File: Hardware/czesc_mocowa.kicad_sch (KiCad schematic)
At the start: 20 parts, among them J1 Screw_Terminal_01x02, J2 Screw_Terminal_01x02, Q1 NMOS, Q2 NMOS, Q3 NMOS, Q4 NMOS, U1 IR2102, U2 IR2102

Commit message: Schemat-update
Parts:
- added C4: C_Polarized, symbol Device:C_Polarized
- added C5, C6: C, symbol Device:C
- added C7: 1nF, symbol Device:C
- added D3: C4D02120A, Package_TO_SOT_THT:TO-220-2_Vertical, symbol Diode:C4D02120A
- added Q5: BC547, Package_TO_SOT_THT:TO-92_Inline, symbol Transistor_BJT:BC547
- added R8: 330R, symbol Device:R
- added U3: LM780_TO220_MA BYC_3V_BO_POJDZIE_Z_DYMEM, Package_TO_SOT_THT:TO-220-3_Vertical, symbol Regulator_Linear:LM7805_TO220
- added U4: STM32L432KCUx, Package_DFN_QFN:QFN-32-1EP_5x5mm_P0.5mm_EP3.45x3.45mm, symbol MCU_ST_STM32L4:STM32L432KCUx
- added U5: ESP32-WROOM-32, RF_Module:ESP32-WROOM-32, symbol RF_Module:ESP32-WROOM-32
- renumbered J1 to WEJ_48V_DC, J2 to WYJSCIE
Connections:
- net GND: now also C3.2, C4.2, C5.2, C6.2, C7.1, Q5.3 (E), U3.2 (GND), U4.16 (VSS), U4.32 (VSS), U4.33 (VSS), U5.1 (GND), U5.15 (GND), U5.38 (GND), U5.39 (GND)
- net at WEJ_48V_DC.1 (Pin_1): now also Q1.1 (D), Q3.1 (D), D3.2 (A); no longer C3.2
- net at Q2.3 (S), Q4.3 (S), R3.1: now also R8.1
- net Logic input 1: no longer names the net of U1.2 (~{HIN})
- net Logic input 1: now also U4.18 (PA8)
- net Logic input 2: no longer names the net of U1.3 (~{LIN})
- net Logic input 2: now also U4.14 (PB0)
- net Logic input 3: no longer names the net of U2.2 (~{HIN})
- net Logic input 3: now also U4.21 (PA11)
- net Logic input 4: no longer names the net of U2.3 (~{LIN})
- net Logic input 4: now also U4.15 (PB1)
- net Vcc: no longer names the net of R6.1, R7.1, U1.1 (VCC), U2.1 (VCC)
- net Vcc: now also C4.1, C6.1, U3.3 (VO), U4.1 (VDD), U4.17 (VDD), U5.2 (VDD)
- new net: C7.2, Q5.2 (B), R8.2
- new net: Q2.2 (G), R2.2
- new net: C3.1, C5.1, D3.1 (K), U3.1 (VI)
- new net RX: U4.30 (PB7), U5.13 (IO14)
- new net TX: U4.29 (PB6), U5.16 (IO13)
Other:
- moved on the sheet: C2, D2, Q3, Q4, R2, R3, R4, R5, R7, U2, WEJ_48V_DC

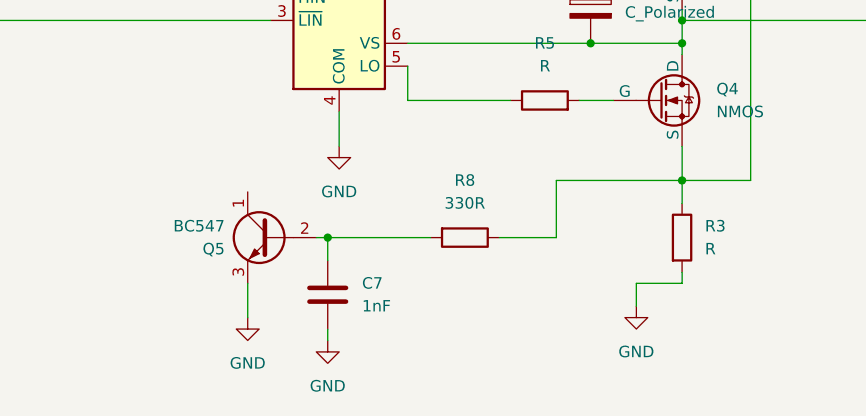
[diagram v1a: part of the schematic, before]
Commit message: Added opamp
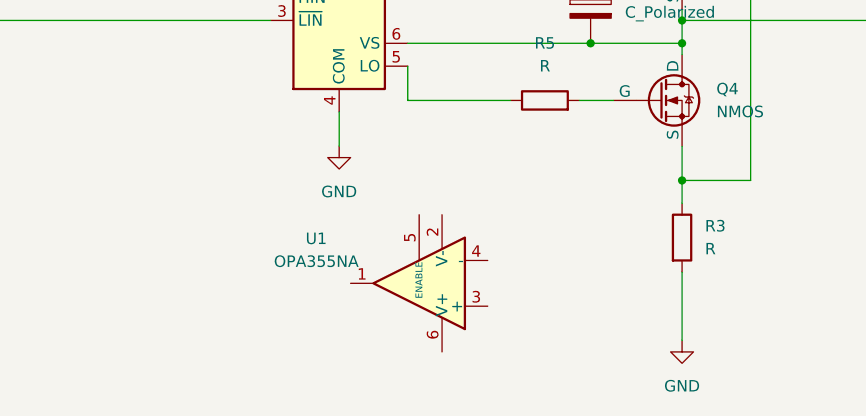
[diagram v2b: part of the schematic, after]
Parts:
- removed C7: 1nF, symbol Device:C
- removed Q5: BC547, Package_TO_SOT_THT:TO-92_Inline, symbol Transistor_BJT:BC547
- removed R8: 330R, symbol Device:R
- added U1: OPA355NA, Package_TO_SOT_SMD:SOT-23-6, symbol Amplifier_Operational:OPA355NA

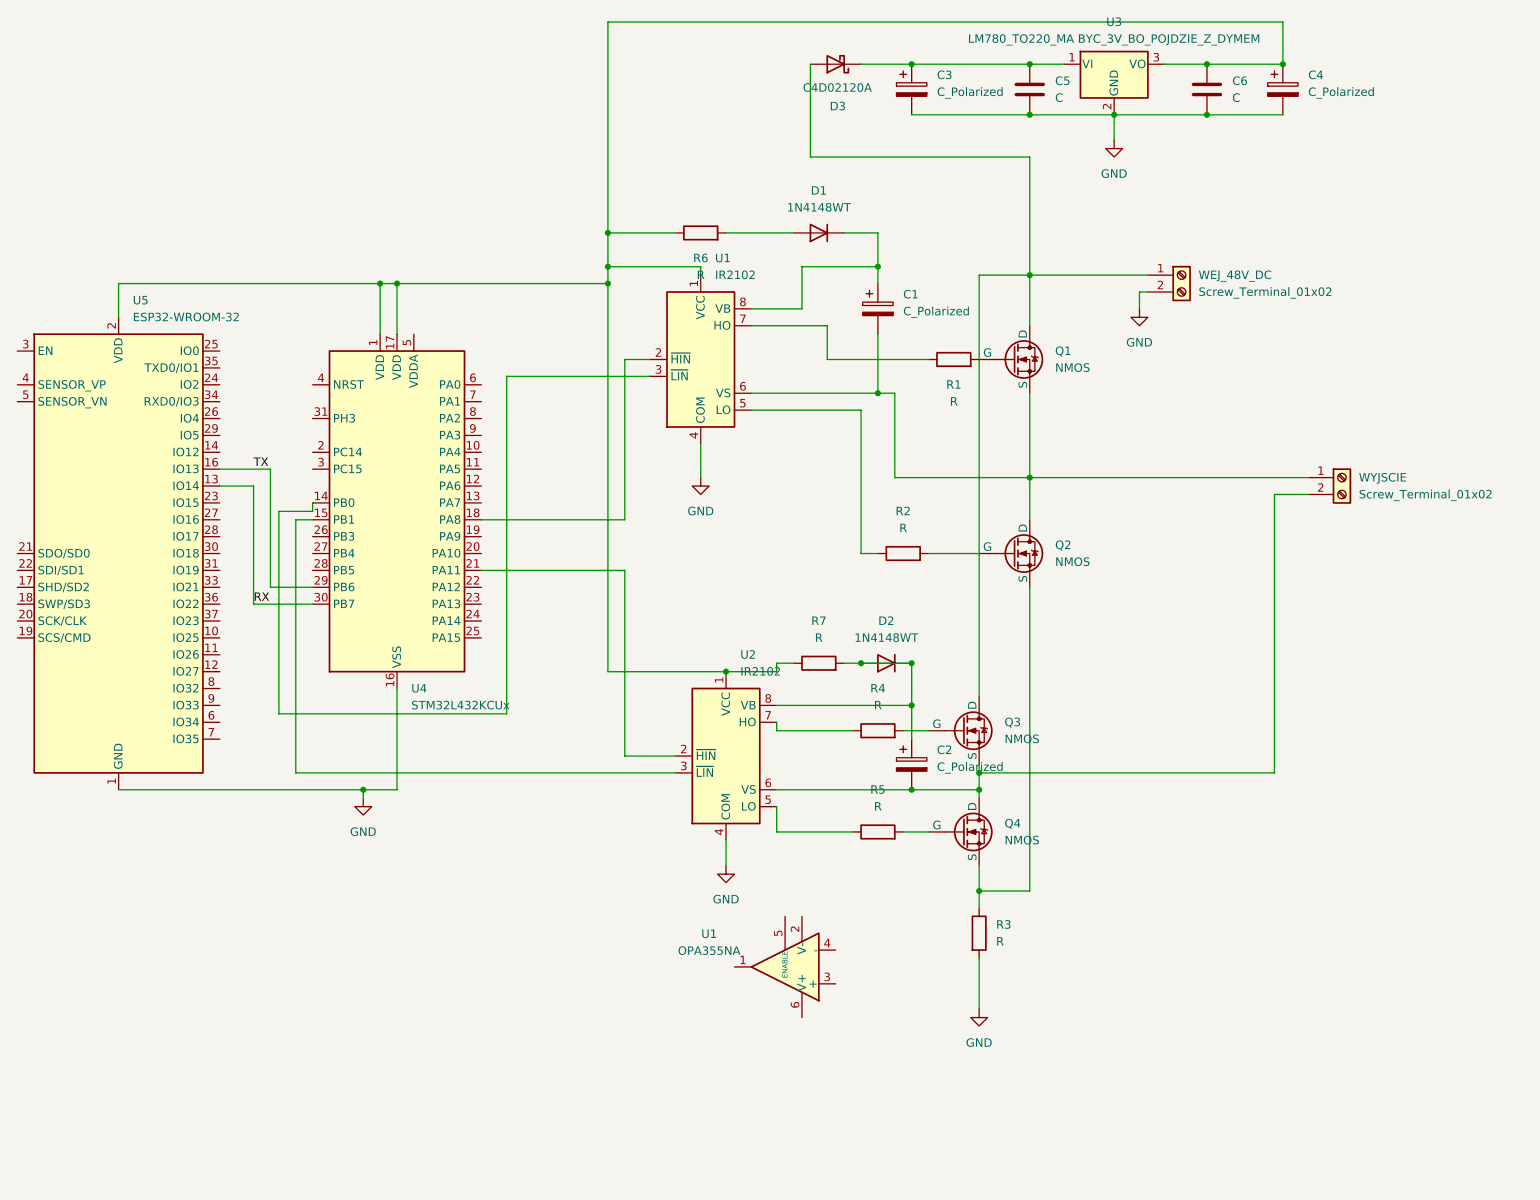
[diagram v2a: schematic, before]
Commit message: Added stm32 project and connect opamp
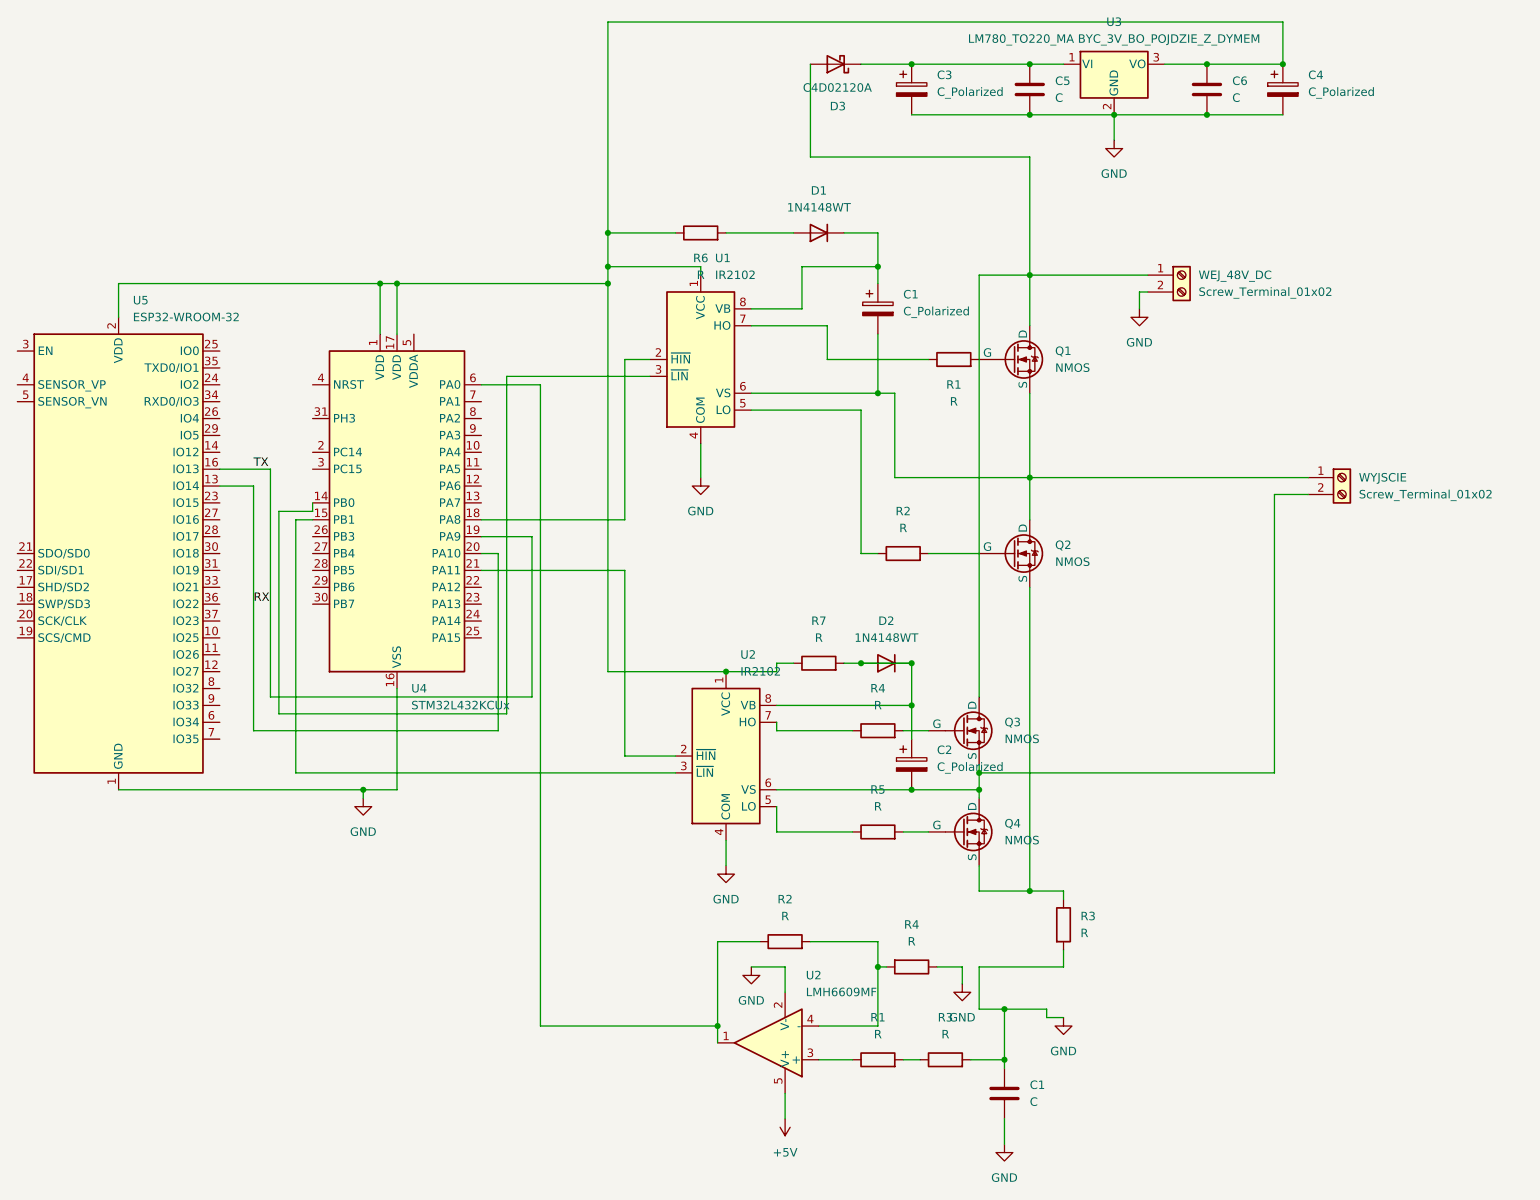
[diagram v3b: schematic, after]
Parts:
- removed U1: OPA355NA, Package_TO_SOT_SMD:SOT-23-6, symbol Amplifier_Operational:OPA355NA
- added C1: C, symbol Device:C
- added R1, R2, R3, R4: R, symbol Device:R
- added U2: LMH6609MF, Package_TO_SOT_SMD:SOT-23-5, symbol Amplifier_Operational:LMH6609MF
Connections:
- net GND: now also C1.1, C1.2, R3.2, R4.1, U2.2 (V-)
- net RX: now also U4.20 (PA10); no longer U4.30 (PB7)
- net TX: now also U4.19 (PA9); no longer U4.29 (PB6)
- net at U4.6 (PA0): now also R2.1, U2.1
- new net: R1.2, R3.1
- new net: R2.2, R4.2, U2.4 (-)
- new net: R1.1, U2.3 (+)
- new net +5V: U2.5 (V+)
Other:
- moved on the sheet: R3

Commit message: KICAD UPDATE
Zmodyfikowałem schemat, finalna wersja
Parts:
- removed R1: R, symbol Device:R
- removed U2: LMH6609MF, Package_TO_SOT_SMD:SOT-23-5, symbol Amplifier_Operational:LMH6609MF
- removed U3: LM780_TO220_MA BYC_3V_BO_POJDZIE_Z_DYMEM, Package_TO_SOT_THT:TO-220-3_Vertical, symbol Regulator_Linear:LM7805_TO220
- added C10, C8: C, symbol Device:C
- added C11, C9: C_Polarized, symbol Device:C_Polarized
- added C7: 1nF, symbol Device:C
- added L1: 5uH, symbol Device:L
- added R8: 10R, symbol Device:R
- added U3: TLV379IDR, Package_TO_SOT_SMD:SOT-23-5, symbol Amplifier_Operational:TLV2371DBV
- added U?: LM780_TO220_MA BYC_3V_BO_POJDZIE_Z_DYMEM, Package_TO_SOT_SMD:SOT-223-3_TabPin2, symbol Regulator_Linear:LD1117S33TR_SOT223
- renumbered C1 to C?, R3 to R?, R4 to R?, R2 to R?
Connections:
- net GND: now also C10.2, C11.2, C7.2, C8.2, C9.2, U3.2 (V-), U?.1 (GND); no longer C?.1, R?.2
- net TX: now also U4.6 (PA0), C7.1, R8.1
- net at Q1.1 (D), Q3.1 (D), WEJ_48V_DC.1 (Pin_1): now also C10.1, C11.1, C8.1, C9.1, L1.2; no longer D3.2 (A)
- net at R?.1: now also U3.3 (+)
- net at C4.1, C6.1, R6.1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: now also U4.5 (VDDA), U3.5 (V+), U?.2 (VO)
- net at Q2.3 (S), Q4.3 (S), R3.1: now also C?.1, R?.2
- net at C3.1, C5.1, D3.1 (K): now also U?.3 (VI)
- net at R?.2, R?.2: now also U3.4 (-)
- net at R?.1: now also R8.2, U3.1; no longer U4.6 (PA0)
- new net: D3.2 (A), L1.1
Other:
- moved on the sheet: C?, R?

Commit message: dodanie footprintów
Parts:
- removed C1: C_Polarized, symbol Device:C_Polarized
- added C13: C, Capacitor_SMD:C_1206_3216Metric, symbol Device:C
- C1: renamed from C?; footprint (none) -> Capacitor_SMD:C_1206_3216Metric
- C10: renamed from C9; value C_Polarized -> 100uF; footprint (none) -> Capacitor_SMD:CP_Elec_10x10
- C11: renamed from C6; value C -> 500pF; footprint (none) -> Capacitor_SMD:C_1206_3216Metric
- C12: renamed from C4; value C_Polarized -> 100uF; footprint (none) -> Capacitor_SMD:CP_Elec_10x10
- C2: renamed from C7; footprint (none) -> Capacitor_SMD:C_1206_3216Metric
- C4: renamed from C3; value C_Polarized -> 100uF; footprint (none) -> Capacitor_SMD:CP_Elec_10x10
- C5: renamed from C2; footprint (none) -> Capacitor_SMD:CP_Elec_5x5.3
- C6: renamed from C5; value C -> 500pF; footprint (none) -> Capacitor_SMD:C_1206_3216Metric
- C7: renamed from C10; footprint (none) -> Capacitor_SMD:C_1206_3216Metric
- C8: footprint (none) -> Capacitor_SMD:C_1206_3216Metric
- C9: renamed from C11; value C_Polarized -> 100uF; footprint (none) -> Capacitor_SMD:CP_Elec_10x10
- L1: footprint (none) -> Inductor_SMD:L_6.3x6.3_H3
- Q1: renamed from Q3; footprint (none) -> Package_TO_SOT_THT:TO-220-3_Horizontal_TabUp
- Q2: renamed from Q4; footprint (none) -> Package_TO_SOT_THT:TO-220-3_Horizontal_TabUp
- Q3: renamed from Q1; footprint (none) -> Package_TO_SOT_THT:TO-220-3_Horizontal_TabUp
- Q4: renamed from Q2; footprint (none) -> Package_TO_SOT_THT:TO-220-3_Horizontal_TabUp
- R1: renamed from R8; footprint (none) -> Resistor_SMD:R_1210_3225Metric
- R10: renamed from R1; footprint (none) -> Resistor_SMD:R_1210_3225Metric
- R11: renamed from R3; footprint (none) -> Resistor_SMD:R_1210_3225Metric
- R2, R3, R4: renamed from R?; footprint (none) -> Resistor_SMD:R_1210_3225Metric
- R5: renamed from R6; footprint (none) -> Resistor_SMD:R_1210_3225Metric
- R6: renamed from R7; footprint (none) -> Resistor_SMD:R_1210_3225Metric
- R7: renamed from R4; footprint (none) -> Resistor_SMD:R_1210_3225Metric
- R8: renamed from R5; footprint (none) -> Resistor_SMD:R_1210_3225Metric
- R9: renamed from R2; footprint (none) -> Resistor_SMD:R_1210_3225Metric
- U1: renamed from U?; footprint Package_TO_SOT_SMD:SOT-223-3_TabPin2 -> Package_TO_SOT_THT:TO-220-3_Horizontal_TabUp
- U4: renamed from U1; footprint (none) -> Package_SO:SOIC-8-1EP_3.9x4.9mm_P1.27mm_EP2.29x3mm
- U5: renamed from U2; footprint (none) -> Package_SO:SOIC-8-1EP_3.9x4.9mm_P1.27mm_EP2.29x3mm
- WEJ_48V_DC1: renamed from WEJ_48V_DC; footprint (none) -> Connector:Banana_Cliff_FCR7350B_S16N-PC_Horizontal
- WYJSCIE1: renamed from WYJSCIE; footprint (none) -> Connector:Banana_Cliff_FCR7350B_S16N-PC_Horizontal
- renumbered D3 to D2, D2 to D3, U5 to U2, U4 to U3, U3 to U6
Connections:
- net at Q3.3 (S), Q4.1 (D), U4.6 (VS)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: now also C13.2
- net at D1.1 (K), U4.8 (VB): now also C13.1
- no-connect marks 0 -> 50

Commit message: Złącza zasilające
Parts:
- removed WEJ_48V_DC1, WYJSCIE1: Screw_Terminal_01x02, Connector:Banana_Cliff_FCR7350B_S16N-PC_Horizontal, symbol Connector:Screw_Terminal_01x02
- added H1, H2: U wyj, symbol Mechanical:MountingHole_Pad
- added H3: +48V Vcc, symbol Mechanical:MountingHole_Pad
- added H4: GND, symbol Mechanical:MountingHole_Pad
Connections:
- net GND: now also H4.1
- net at C10.1, C7.1, C8.1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: now also H3.1
- net at C13.2, Q3.3 (S), Q4.1 (D)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: now also H1.1
- net at C5.2, Q1.3 (S), Q2.1 (D)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: now also H2.1

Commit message: Added PCB
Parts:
- H1, H2, H3, H4: footprint (none) -> MountingHole:MountingHole_3.2mm_M3_DIN965_Pad
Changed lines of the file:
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@@
 			)
 		)
-		(property "Footprint" ""
+		(property "Footprint" "MountingHole:MountingHole_3.2mm_M3_DIN965_Pad"
 			(at 215.9 88.9 0)
 			(effects
@@
 			)
 		)
-		(property "Footprint" ""
+		(property "Footprint" "MountingHole:MountingHole_3.2mm_M3_DIN965_Pad"
 			(at 215.9 80.01 0)
 			(effects
@@
 			)
 		)
-		(property "Footprint" ""
+		(property "Footprint" "MountingHole:MountingHole_3.2mm_M3_DIN965_Pad"
 			(at 208.28 50.8 0)
 			(effects
@@
 			)
 		)
-		(property "Footprint" ""
+		(property "Footprint" "MountingHole:MountingHole_3.2mm_M3_DIN965_Pad"
 			(at 208.28 58.42 0)
 			(effects
